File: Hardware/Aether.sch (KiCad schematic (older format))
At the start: 13 parts, among them J1 PRGM, J2 CONN-2, J3 CONN-2, J4 CONN-2, J5 CONN-2, J6 CONN-3, J7 CONN-3

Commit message: GPS components
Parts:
- D1: value LED -> STAT; footprint ~ -> LEDC1608-N; Current I -> 20mA; Distributor Part No (none) -> 475-3016-1-ND; MFR Name (none) -> Osram; MFR Part No (none) -> LS Q971-KN-1; Voltage V -> 1.9V
- D2: value LED -> PWR; footprint ~ -> LEDC1608-N; Current I -> 20mA; Distributor Part No (none) -> 475-1409-1-ND; MFR Name (none) -> Osram; MFR Part No (none) -> LG Q971-KN-1; Voltage V -> 2.2V
- R1, R2: value R -> 120; footprint ~ -> RESC1608-N; Distributor Part No (none) -> RHM120DCT-ND; MFR Name (none) -> Rohm; MFR Part No (none) -> ESR03EZPJ121; Power W -> 1/8W; Tolerance % -> 5%
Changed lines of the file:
@@
 	5200 3800 4200 3800
-$Comp
-L R R2
-U 1 1 52EF8E3F
-P 7300 5050
-F 0 "R2" H 7300 5150 50  0000 C CNN
-F 1 "R" H 7300 5050 50  0000 C CNN
-F 2 "~" H 7300 5050 60  0000 C CNN
-F 3 "~" H 7300 5050 60  0000 C CNN
-F 4 "W" H 7300 4950 50  0001 C CNN "Power"
-F 5 "%" H 7300 4850 50  0001 C CNN "Tolerance"
-	1    7300 5050
-	0    -1   -1   0
-$EndComp
 $Comp
 L LED D2
@@
 P 7300 5650
 F 0 "D2" H 7300 5775 60  0000 C CNN
-F 1 "LED" H 7300 5550 60  0000 C CNN
-F 2 "~" H 7300 5650 60  0000 C CNN
+F 1 "PWR" H 7300 5550 60  0000 C CNN
+F 2 "LEDC1608-N" H 7300 5650 60  0001 C CNN
 F 3 "~" H 7300 5650 60  0000 C CNN
-F 4 "V" H 7700 6175 60  0001 C CNN "Voltage"
-F 5 "I" H 7800 6275 60  0001 C CNN "Current"
+F 4 "Osram" H 7300 5650 60  0001 C CNN "MFR Name"
+F 5 "LG Q971-KN-1" H 7300 5650 60  0001 C CNN "MFR Part No"
+F 6 "475-1409-1-ND" H 7300 5650 60  0001 C CNN "Distributor Part No"
+F 7 "2.2V" H 7700 6175 60  0001 C CNN "Voltage"
+F 8 "20mA" H 7800 6275 60  0001 C CNN "Current"
 	1    7300 5650
 	0    1    1    0
@@
 P 6900 5650
 F 0 "D1" H 6900 5775 60  0000 C CNN
-F 1 "LED" H 6900 5550 60  0000 C CNN
-F 2 "~" H 6900 5650 60  0000 C CNN
+F 1 "STAT" H 6900 5550 60  0000 C CNN
+F 2 "LEDC1608-N" H 6900 5650 60  0001 C CNN
 F 3 "~" H 6900 5650 60  0000 C CNN
-F 4 "V" H 7300 6175 60  0001 C CNN "Voltage"
-F 5 "I" H 7400 6275 60  0001 C CNN "Current"
+F 4 "Osram" H 6900 5650 60  0001 C CNN "MFR Name"
+F 5 "LS Q971-KN-1" H 6900 5650 60  0001 C CNN "MFR Part No"
+F 6 "475-3016-1-ND" H 6900 5650 60  0001 C CNN "Distributor Part No"
+F 7 "1.9V" H 7300 6175 60  0001 C CNN "Voltage"
+F 8 "20mA" H 7400 6275 60  0001 C CNN "Current"
 	1    6900 5650
 	0    1    1    0
@@
 P 6900 5050
 F 0 "R1" H 6900 5150 50  0000 C CNN
-F 1 "R" H 6900 5050 50  0000 C CNN
-F 2 "~" H 6900 5050 60  0000 C CNN
+F 1 "120" H 6900 5050 50  0000 C CNN
+F 2 "RESC1608-N" H 6900 5050 60  0001 C CNN
 F 3 "~" H 6900 5050 60  0000 C CNN
-F 4 "W" H 6900 4950 50  0001 C CNN "Power"
-F 5 "%" H 6900 4850 50  0001 C CNN "Tolerance"
+F 4 "Rohm" H 6900 5050 60  0001 C CNN "MFR Name"
+F 5 "ESR03EZPJ121" H 6900 5050 60  0001 C CNN "MFR Part No"
+F 6 "RHM120DCT-ND" H 6900 5050 60  0001 C CNN "Distributor Part No"
+F 7 "1/8W" H 6900 4950 50  0001 C CNN "Power"
+F 8 "5%" H 6900 4850 50  0001 C CNN "Tolerance"
 	1    6900 5050
 	0    -1   -1   0
@@
 Wire Wire Line
 	3100 2100 3200 2100
+$Comp
+L R R2
+U 1 1 52F5ABE2
+P 7300 5050
+F 0 "R2" H 7300 5150 50  0000 C CNN
+F 1 "120" H 7300 5050 50  0000 C CNN
+F 2 "RESC1608-N" H 7300 5050 60  0001 C CNN
+F 3 "~" H 7300 5050 60  0000 C CNN
+F 4 "Rohm" H 7300 5050 60  0001 C CNN "MFR Name"
+F 5 "ESR03EZPJ121" H 7300 5050 60  0001 C CNN "MFR Part No"
+F 6 "RHM120DCT-ND" H 7300 5050 60  0001 C CNN "Distributor Part No"
+F 7 "1/8W" H 7300 4950 50  0001 C CNN "Power"
+F 8 "5%" H 7300 4850 50  0001 C CNN "Tolerance"
+	1    7300 5050
+	0    -1   -1   0
+$EndComp
 $EndSCHEMATC

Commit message: Majority of layout
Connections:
- net Core/E2: now reaches J3.1
- net Core/E1: now reaches J3.2
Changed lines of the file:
@@
 Sheet 1 4
 Title "Aether - Pico Tracker"
-Date "8 feb 2014"
+Date "9 feb 2014"
 Rev "1"
 Comp "Aerodyne Labs"
@@
 Comment4 ""
 $EndDescr
-$Sheet
-S 3200 3300 1000 1000
-U 52E9B1A2
-F0 "GPS" 50
-F1 "GPS.sch" 50
-F2 "TX" O R 4200 3400 60
-F3 "RX" I R 4200 3500 60
-F4 "GPS_En" I R 4200 3700 60
-F5 "GPS_Perf" I R 4200 3800 60
-$EndSheet
 $Sheet
 S 7200 3300 1000 1000
@@
 Connection ~ 8900 3800
 Wire Wire Line
-	4200 3400 5200 3400
-Wire Wire Line
-	4200 3500 5200 3500
-Wire Wire Line
-	4200 3700 5200 3700
+	4200 4000 5200 4000
 $Comp
 L BATTERY B1
@@
 $EndComp
 Wire Wire Line
-	4400 5700 4400 3400
-Connection ~ 4400 3400
-Wire Wire Line
-	4500 5800 4500 3500
-Connection ~ 4500 3500
+	4400 5700 4400 3700
+Connection ~ 4400 3700
+Wire Wire Line
+	4500 5800 4500 3800
+Connection ~ 4500 3800
 Wire Wire Line
 	4800 5500 4800 4500
@@
 	5000 5900 5000 4700
 Wire Wire Line
-	5200 3800 4200 3800
+	5200 4100 4200 4100
 $Comp
 L LED D2
@@
 F0 "Core" 50
 F1 "Core.sch" 50
-F2 "RX" I L 5200 3400 60
-F3 "TX" O L 5200 3500 60
-F4 "GPS_En" O L 5200 3700 60
+F2 "RX" I L 5200 3700 60
+F3 "TX" O L 5200 3800 60
+F4 "GPS_En" O L 5200 4000 60
 F5 "TDIO/RST" B L 5200 4500 60
 F6 "TCK/TEST" I L 5200 4700 60
 F7 "PGM_Det" I L 5200 4600 60
-F8 "GPS_Perf" O L 5200 3800 60
+F8 "GPS_Perf" O L 5200 4100 60
 F9 "Stat" O R 6200 4700 60
 F10 "SDA" B R 6200 3500 60
@@
 F17 "CLK_En" O R 6200 4100 60
 F18 "MOSI" O R 6200 3800 60
+F19 "E1" B L 5200 3400 60
+F20 "E2" B L 5200 3500 60
 $EndSheet
 $Comp
@@
 F 3 "~" H 3900 2150 60  0000 C CNN
 	1    3900 2150
-	1    0    0    -1
+	1    0    0    1
 $EndComp
 $Comp
@@
 	0    -1   -1   0
 $EndComp
+$Sheet
+S 3200 3300 1000 1000
+U 52E9B1A2
+F0 "GPS" 50
+F1 "GPS.sch" 50
+F2 "TX" O R 4200 3700 60
+F3 "RX" I R 4200 3800 60
+F4 "GPS_En" I R 4200 4000 60
+F5 "GPS_Perf" I R 4200 4100 60
+$EndSheet
+Wire Wire Line
+	4200 3700 5200 3700
+Wire Wire Line
+	4200 3800 5200 3800
+Wire Wire Line
+	5200 3400 4800 3400
+Wire Wire Line
+	4800 3400 4800 2100
+Wire Wire Line
+	4800 2100 4200 2100
+Wire Wire Line
+	4200 2200 4700 2200
+Wire Wire Line
+	4700 2200 4700 3500
+Wire Wire Line
+	4700 3500 5200 3500
 $EndSCHEMATC

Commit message: Consolidate LED resistors
See #1
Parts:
- B1: Distributor Part No (none) -> BK-92-ND; MFR Name (none) -> MPD; MFR Part No (none) -> BK-92
- R1, R2: footprint RESC1608-N -> RESC1005_N; Distributor Part No RHM120DCT-ND -> 1276-4354-1-ND; MFR Name Rohm -> Samsung; MFR Part No ESR03EZPJ121 -> RC1005J121CS; Power 1/8W -> 1/16W
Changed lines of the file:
@@
 Sheet 1 4
 Title "Aether - Pico Tracker"
-Date "9 feb 2014"
+Date "24 feb 2014"
 Rev "1"
 Comp "Aerodyne Labs"
@@
 F 2 "BATT-AA-BK92" H 7700 5350 60  0001 C CNN
 F 3 "~" H 7700 5350 60  0000 C CNN
+F 4 "MPD" H 7700 5350 60  0001 C CNN "MFR Name"
+F 5 "BK-92" H 7700 5350 60  0001 C CNN "MFR Part No"
+F 6 "BK-92-ND" H 7700 5350 60  0001 C CNN "Distributor Part No"
 	1    7700 5350
 	1    0    0    -1
@@
 F 0 "R1" H 6900 5150 50  0000 C CNN
 F 1 "120" H 6900 5050 50  0000 C CNN
-F 2 "RESC1608-N" H 6900 5050 60  0001 C CNN
+F 2 "RESC1005_N" H 6900 5050 60  0001 C CNN
 F 3 "~" H 6900 5050 60  0000 C CNN
-F 4 "Rohm" H 6900 5050 60  0001 C CNN "MFR Name"
-F 5 "ESR03EZPJ121" H 6900 5050 60  0001 C CNN "MFR Part No"
-F 6 "RHM120DCT-ND" H 6900 5050 60  0001 C CNN "Distributor Part No"
-F 7 "1/8W" H 6900 4950 50  0001 C CNN "Power"
+F 4 "Samsung" H 6900 5050 60  0001 C CNN "MFR Name"
+F 5 "RC1005J121CS" H 6900 5050 60  0001 C CNN "MFR Part No"
+F 6 "1276-4354-1-ND" H 6900 5050 60  0001 C CNN "Distributor Part No"
+F 7 "1/16W" H 6900 4950 50  0001 C CNN "Power"
 F 8 "5%" H 6900 4850 50  0001 C CNN "Tolerance"
 	1    6900 5050
@@
 Wire Wire Line
 	3100 2100 3200 2100
-$Comp
-L R R2
-U 1 1 52F5ABE2
-P 7300 5050
-F 0 "R2" H 7300 5150 50  0000 C CNN
-F 1 "120" H 7300 5050 50  0000 C CNN
-F 2 "RESC1608-N" H 7300 5050 60  0001 C CNN
-F 3 "~" H 7300 5050 60  0000 C CNN
-F 4 "Rohm" H 7300 5050 60  0001 C CNN "MFR Name"
-F 5 "ESR03EZPJ121" H 7300 5050 60  0001 C CNN "MFR Part No"
-F 6 "RHM120DCT-ND" H 7300 5050 60  0001 C CNN "Distributor Part No"
-F 7 "1/8W" H 7300 4950 50  0001 C CNN "Power"
-F 8 "5%" H 7300 4850 50  0001 C CNN "Tolerance"
-	1    7300 5050
-	0    -1   -1   0
-$EndComp
 $Sheet
 S 3200 3300 1000 1000
@@
 Wire Wire Line
 	4700 3500 5200 3500
+$Comp
+L R R2
+U 1 1 530ACC2A
+P 7300 5050
+F 0 "R2" H 7300 5150 50  0000 C CNN
+F 1 "120" H 7300 5050 50  0000 C CNN
+F 2 "RESC1005_N" H 7300 5050 60  0001 C CNN
+F 3 "~" H 7300 5050 60  0000 C CNN
+F 4 "Samsung" H 7300 5050 60  0001 C CNN "MFR Name"
+F 5 "RC1005J121CS" H 7300 5050 60  0001 C CNN "MFR Part No"
+F 6 "1276-4354-1-ND" H 7300 5050 60  0001 C CNN "Distributor Part No"
+F 7 "1/16W" H 7300 4950 50  0001 C CNN "Power"
+F 8 "5%" H 7300 4850 50  0001 C CNN "Tolerance"
+	1    7300 5050
+	0    -1   -1   0
+$EndComp
 $EndSCHEMATC

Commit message: Prepare for r2
Delete board, netlist, associations
Clear annotations
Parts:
- renumbered AE1 to AE?, B1 to B?, D2 to D?, D1 to D?, J1 to J?, J5 to J?, J4 to J?, J3 to J?, J2 to J?, J7 to J?, J6 to J?, R1 to R?, R2 to R?
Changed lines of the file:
@@
 $EndSheet
 $Comp
-L ANTENNA AE1
+L ANTENNA AE?
 U 1 1 52E9D9F3
 P 9200 3500
-F 0 "AE1" H 9200 3650 60  0000 C CNN
+F 0 "AE?" H 9200 3650 60  0000 C CNN
 F 1 "ANTENNA" V 9250 3350 60  0000 R CNN
 F 2 "SMA_Edge" H 9200 3500 60  0001 C CNN
@@
 	4200 4000 5200 4000
 $Comp
-L BATTERY B1
+L BATTERY B?
 U 1 1 52EDBE30
 P 7700 5350
-F 0 "B1" H 7850 5500 60  0000 C CNN
+F 0 "B?" H 7850 5500 60  0000 C CNN
 F 1 "AA" H 7850 5200 60  0000 C CNN
 F 2 "BATT-AA-BK92" H 7700 5350 60  0001 C CNN
@@
 $EndComp
 $Comp
-L GND #PWR01
+L GND #PWR?
 U 1 1 52EDBF2F
 P 7700 5700
-F 0 "#PWR01" H 7700 5700 30  0001 C CNN
+F 0 "#PWR?" H 7700 5700 30  0001 C CNN
 F 1 "GND" H 7700 5630 30  0001 C CNN
 F 2 "" H 7700 5700 60  0000 C CNN
@@
 $EndComp
 $Comp
-L +BATT #PWR02
+L +BATT #PWR?
 U 1 1 52EDBFF2
 P 7700 5000
-F 0 "#PWR02" H 7700 4950 20  0001 C CNN
+F 0 "#PWR?" H 7700 4950 20  0001 C CNN
 F 1 "+BATT" H 7700 5100 30  0000 C CNN
 F 2 "" H 7700 5000 60  0000 C CNN
@@
 	7700 5600 7700 5700
 $Comp
-L CONN-6 J1
+L CONN-6 J?
 U 1 1 52EDCAB3
 P 3500 5650
-F 0 "J1" H 3500 6000 60  0000 C CNN
+F 0 "J?" H 3500 6000 60  0000 C CNN
 F 1 "PRGM" H 3500 5300 60  0000 C CNN
 F 2 "HDRV6W38P254_6X1-LOCK" H 3500 5650 60  0001 C CNN
@@
 	3900 5400 4000 5400
 $Comp
-L +5V #PWR03
+L +5V #PWR?
 U 1 1 52EDCABF
 P 4100 5300
-F 0 "#PWR03" H 4100 5390 20  0001 C CNN
+F 0 "#PWR?" H 4100 5390 20  0001 C CNN
 F 1 "+5V" H 4100 5390 30  0000 C CNN
 F 2 "" H 4100 5300 60  0000 C CNN
@@
 $EndComp
 $Comp
-L GND #PWR04
+L GND #PWR?
 U 1 1 52EDCAB9
 P 4000 6000
-F 0 "#PWR04" H 4000 6000 30  0001 C CNN
+F 0 "#PWR?" H 4000 6000 30  0001 C CNN
 F 1 "GND" H 4000 5930 30  0001 C CNN
 F 2 "" H 4000 6000 60  0000 C CNN
@@
 	5200 4100 4200 4100
 $Comp
-L LED D2
+L LED D?
 U 1 1 52EF8E5A
 P 7300 5650
-F 0 "D2" H 7300 5775 60  0000 C CNN
+F 0 "D?" H 7300 5775 60  0000 C CNN
 F 1 "PWR" H 7300 5550 60  0000 C CNN
 F 2 "LEDC1608-N" H 7300 5650 60  0001 C CNN
@@
 $EndComp
 $Comp
-L LED D1
+L LED D?
 U 1 1 52EF8F5F
 P 6900 5650
-F 0 "D1" H 6900 5775 60  0000 C CNN
+F 0 "D?" H 6900 5775 60  0000 C CNN
 F 1 "STAT" H 6900 5550 60  0000 C CNN
 F 2 "LEDC1608-N" H 6900 5650 60  0001 C CNN
@@
 $EndComp
 $Comp
-L R R1
+L R R?
 U 1 1 52EF8FE3
 P 6900 5050
-F 0 "R1" H 6900 5150 50  0000 C CNN
+F 0 "R?" H 6900 5150 50  0000 C CNN
 F 1 "120" H 6900 5050 50  0000 C CNN
 F 2 "RESC1005_N" H 6900 5050 60  0001 C CNN
@@
 $EndComp
 $Comp
-L +3.3V #PWR05
+L +3.3V #PWR?
 U 1 1 52EF9184
 P 7300 4700
-F 0 "#PWR05" H 7300 4660 30  0001 C CNN
+F 0 "#PWR?" H 7300 4660 30  0001 C CNN
 F 1 "+3.3V" H 7300 4810 30  0000 C CNN
 F 2 "" H 7300 4700 60  0000 C CNN
@@
 	7300 4700 7300 4800
 $Comp
-L GND #PWR06
+L GND #PWR?
 U 1 1 52EF9208
 P 7300 6000
-F 0 "#PWR06" H 7300 6000 30  0001 C CNN
+F 0 "#PWR?" H 7300 6000 30  0001 C CNN
 F 1 "GND" H 7300 5930 30  0001 C CNN
 F 2 "" H 7300 6000 60  0000 C CNN
@@
 $EndComp
 $Comp
-L GND #PWR07
+L GND #PWR?
 U 1 1 52EF9217
 P 6900 6000
-F 0 "#PWR07" H 6900 6000 30  0001 C CNN
+F 0 "#PWR?" H 6900 6000 30  0001 C CNN
 F 1 "GND" H 6900 5930 30  0001 C CNN
 F 2 "" H 6900 6000 60  0000 C CNN
@@
 $EndSheet
 $Comp
-L CONN-2 J5
+L CONN-2 J?
 U 1 1 52F23BAF
 P 5900 2150
-F 0 "J5" H 5900 2300 60  0000 C CNN
+F 0 "J?" H 5900 2300 60  0000 C CNN
 F 1 "CONN-2" H 5900 2000 60  0000 C CNN
 F 2 "~" H 5900 2150 60  0000 C CNN
@@
 $EndComp
 $Comp
-L CONN-2 J4
+L CONN-2 J?
 U 1 1 52F23CB1
 P 5500 2150
-F 0 "J4" H 5500 2300 60  0000 C CNN
+F 0 "J?" H 5500 2300 60  0000 C CNN
 F 1 "CONN-2" H 5500 2000 60  0000 C CNN
 F 2 "~" H 5500 2150 60  0000 C CNN
@@
 	6200 2100 6500 2100
 $Comp
-L GND #PWR08
+L GND #PWR?
 U 1 1 52F23EE7
 P 5100 2300
-F 0 "#PWR08" H 5100 2300 30  0001 C CNN
+F 0 "#PWR?" H 5100 2300 30  0001 C CNN
 F 1 "GND" H 5100 2230 30  0001 C CNN
 F 2 "" H 5100 2300 60  0000 C CNN
@@
 $EndComp
 $Comp
-L +3.3V #PWR09
+L +3.3V #PWR?
 U 1 1 52F23EF6
 P 5100 2000
-F 0 "#PWR09" H 5100 1960 30  0001 C CNN
+F 0 "#PWR?" H 5100 1960 30  0001 C CNN
 F 1 "+3.3V" H 5100 2110 30  0000 C CNN
 F 2 "" H 5100 2000 60  0000 C CNN
@@
 	8600 3500 8900 3500
 $Comp
-L GND #PWR010
+L GND #PWR?
 U 1 1 52F2542B
 P 6900 2300
-F 0 "#PWR010" H 6900 2300 30  0001 C CNN
+F 0 "#PWR?" H 6900 2300 30  0001 C CNN
 F 1 "GND" H 6900 2230 30  0001 C CNN
 F 2 "" H 6900 2300 60  0000 C CNN
@@
 Connection ~ 8700 3700
 $Comp
-L CONN-2 J3
+L CONN-2 J?
 U 1 1 52F263D4
 P 3900 2150
-F 0 "J3" H 3900 2300 60  0000 C CNN
+F 0 "J?" H 3900 2300 60  0000 C CNN
 F 1 "CONN-2" H 3900 2000 60  0000 C CNN
 F 2 "~" H 3900 2150 60  0000 C CNN
@@
 $EndComp
 $Comp
-L CONN-2 J2
+L CONN-2 J?
 U 1 1 52F26485
 P 3500 2150
-F 0 "J2" H 3500 2300 60  0000 C CNN
+F 0 "J?" H 3500 2300 60  0000 C CNN
 F 1 "CONN-2" H 3500 2000 60  0000 C CNN
 F 2 "~" H 3500 2150 60  0000 C CNN
@@
 $EndComp
 $Comp
-L CONN-3 J7
+L CONN-3 J?
 U 1 1 52F26D74
 P 8000 2100
-F 0 "J7" H 8000 2300 60  0000 C CNN
+F 0 "J?" H 8000 2300 60  0000 C CNN
 F 1 "CONN-3" H 8000 1900 60  0000 C CNN
 F 2 "~" H 8000 2050 60  0000 C CNN
@@
 $EndComp
 $Comp
-L CONN-3 J6
+L CONN-3 J?
 U 1 1 52F26D83
 P 7400 2100
-F 0 "J6" H 7400 2300 60  0000 C CNN
+F 0 "J?" H 7400 2300 60  0000 C CNN
 F 1 "CONN-3" H 7400 1900 60  0000 C CNN
 F 2 "~" H 7400 2050 60  0000 C CNN
@@
 Connection ~ 6800 3600
 $Comp
-L +BATT #PWR011
+L +BATT #PWR?
 U 1 1 52F2F27B
 P 6900 1900
-F 0 "#PWR011" H 6900 1850 20  0001 C CNN
+F 0 "#PWR?" H 6900 1850 20  0001 C CNN
 F 1 "+BATT" H 6900 2000 30  0000 C CNN
 F 2 "" H 6900 1900 60  0000 C CNN
@@
 	6900 2000 7000 2000
 $Comp
-L +BATT #PWR012
+L +BATT #PWR?
 U 1 1 52F2F5FA
 P 3100 2000
-F 0 "#PWR012" H 3100 1950 20  0001 C CNN
+F 0 "#PWR?" H 3100 1950 20  0001 C CNN
 F 1 "+BATT" H 3100 2100 30  0000 C CNN
 F 2 "" H 3100 2000 60  0000 C CNN
@@
 $EndComp
 $Comp
-L GND #PWR013
+L GND #PWR?
 U 1 1 52F2F609
 P 3100 2300
-F 0 "#PWR013" H 3100 2300 30  0001 C CNN
+F 0 "#PWR?" H 3100 2300 30  0001 C CNN
 F 1 "GND" H 3100 2230 30  0001 C CNN
 F 2 "" H 3100 2300 60  0000 C CNN
@@
 	4700 3500 5200 3500
 $Comp
-L R R2
+L R R?
 U 1 1 530ACC2A
 P 7300 5050
-F 0 "R2" H 7300 5150 50  0000 C CNN
+F 0 "R?" H 7300 5150 50  0000 C CNN
 F 1 "120" H 7300 5050 50  0000 C CNN
 F 2 "RESC1005_N" H 7300 5050 60  0001 C CNN

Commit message: Prepare for new GPS
Remove connections to subsheet
Clear subsheet
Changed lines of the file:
@@
 Sheet 1 4
 Title "Aether - Pico Tracker"
-Date "25 feb 2014"
+Date "29 jun 2014"
 Rev "1"
 Comp "Aerodyne Labs"
@@
 	8900 3900 9000 3900
 Connection ~ 8900 3800
-Wire Wire Line
-	4200 4000 5200 4000
 $Comp
 L BATTERY B?
@@
 Wire Wire Line
 	4400 5700 4400 3700
-Connection ~ 4400 3700
 Wire Wire Line
 	4500 5800 4500 3800
-Connection ~ 4500 3800
 Wire Wire Line
 	4800 5500 4800 4500
@@
 Wire Wire Line
 	5000 5900 5000 4700
-Wire Wire Line
-	5200 4100 4200 4100
 $Comp
 L LED D?
@@
 F2 "TX" O R 4200 3700 60
 F3 "RX" I R 4200 3800 60
-F4 "GPS_En" I R 4200 4000 60
-F5 "GPS_Perf" I R 4200 4100 60
 $EndSheet
-Wire Wire Line
-	4200 3700 5200 3700
-Wire Wire Line
-	4200 3800 5200 3800
 Wire Wire Line
 	5200 3400 4800 3400
@@
 	0    -1   -1   0
 $EndComp
+Wire Wire Line
+	4500 3800 5200 3800
+Wire Wire Line
+	4400 3700 5200 3700
 $EndSCHEMATC

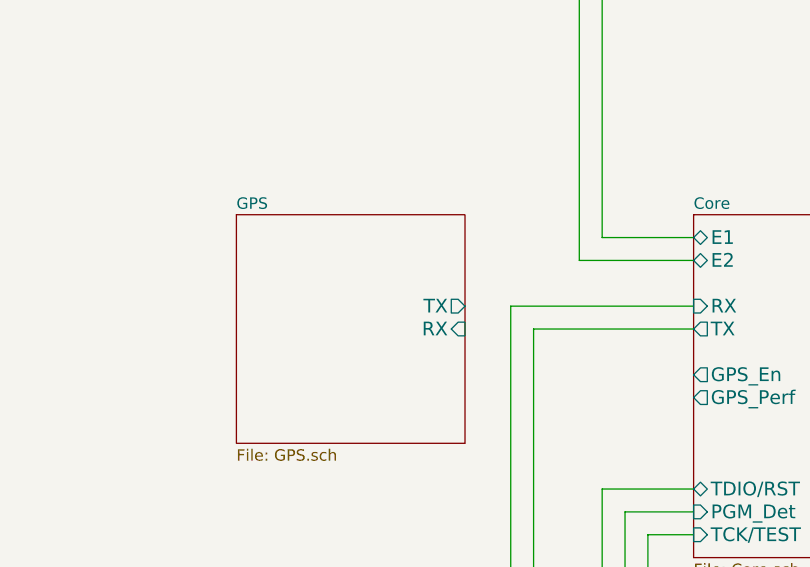
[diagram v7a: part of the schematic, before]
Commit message: Add Venus838 to schematic
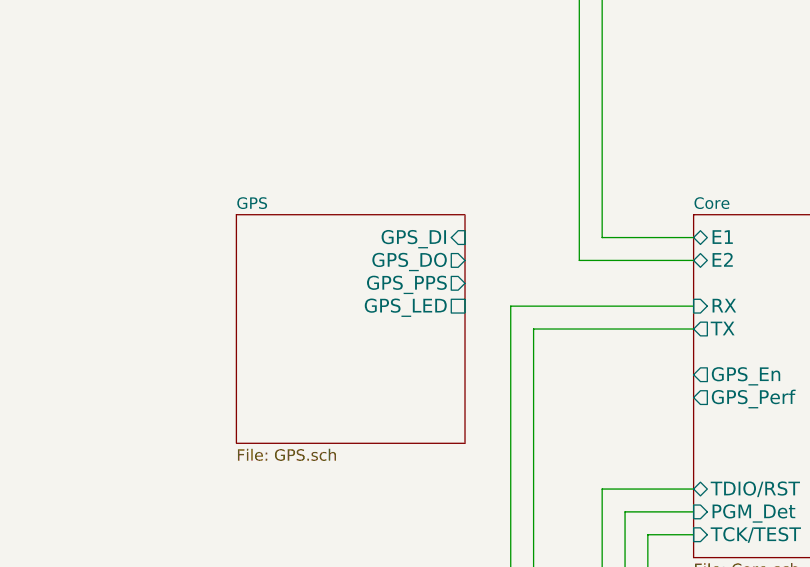
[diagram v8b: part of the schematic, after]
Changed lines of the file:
@@
 F0 "GPS" 50
 F1 "GPS.sch" 50
-F2 "TX" O R 4200 3700 60
-F3 "RX" I R 4200 3800 60
+F2 "GPS_DI" I R 4200 3400 60
+F3 "GPS_DO" O R 4200 3500 60
+F4 "GPS_LED" U R 4200 3700 60
+F5 "GPS_PPS" O R 4200 3600 60
 $EndSheet
 Wire Wire Line
